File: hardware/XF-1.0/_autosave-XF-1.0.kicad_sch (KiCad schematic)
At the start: 9 parts

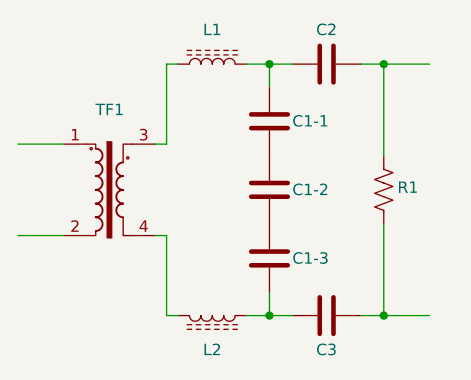
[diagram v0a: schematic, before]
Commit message: modified:   README.md 	new file:   hardware/XF-1.0/#auto_saved_files# 	new file:   hardware/XF-1.0/XF-1.0-backups/XF-1.0-2025-07-15_095716.zip 	modified:   hardware/XF-1.0/XF-1.0.kicad_sch 	new file:   hardware/XF-1.0/_autosave-XF-1.0.kicad_sch
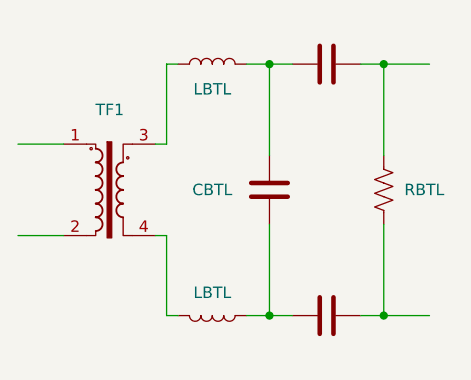
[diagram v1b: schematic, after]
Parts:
- removed C1-2, C1-3: 1nF, Capacitor_THT:C_Rect_L13.0mm_W8.0mm_P10.00mm_FKS3_FKP3_MKS4, symbol Device:C
- removed L1, L2: ~, Transformer_THT:Inductor-EE25, symbol Device:L_Ferrite
- added L1, L2: LBTL, symbol Device:L
- C3: renamed from C1-1; value 1nF -> CBTL
- R1: value R_US -> RBTL
- renumbered C2 to C1, C3 to C2
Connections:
- net at C2.1: now also C3.2, L2.2
- net at TF1.3: now also L1.1
- net at TF1.4: now also L2.1
- net at C1.1, C3.1: now also L1.2
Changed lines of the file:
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@@
 	(wire
 		(pts
-			(xy 149.86 59.69) (xy 149.86 62.23)
+			(xy 149.86 59.69) (xy 149.86 69.85)
 		)
 		(stroke
@@
 	(wire
 		(pts
+			(xy 149.86 77.47) (xy 149.86 87.63)
+		)
+		(stroke
+			(width 0)
+			(type default)
+		)
+	)
+	(wire
+		(pts
 			(xy 147.32 87.63) (xy 149.86 87.63)
 		)
@@
 		(pts
 			(xy 138.43 68.58) (xy 137.16 68.58)
-		)
-		(stroke
-			(width 0)
-			(type default)
-		)
-	)
-	(wire
-		(pts
-			(xy 149.86 85.09) (xy 149.86 87.63)
 		)
 		(stroke
@@
 		(on_board yes)
 		(dnp no)
-		(property "Reference" "C3"
+		(property "Reference" "C2"
 			(at 156.21 91.44 90)
 			(effects
@@
 					(size 1.27 1.27)
 				)
+				(hide yes)
 			)
 		)
@@
 			(project "XF-1.0"
 				(path "/12f985fe-55a3-431b-9b29-de85666dcd2b"
-					(reference "C3")
+					(reference "C2")
 					(unit 1)
 				)
@@
 	(symbol
 		(lib_id "Device:C")
-		(at 149.86 66.04 0)
-		(unit 1)
-		(exclude_from_sim no)
-		(in_bom yes)
-		(on_board yes)
-		(dnp no)
-		(property "Reference" "C1-1"
-			(at 152.4 66.04 0)
-			(effects
-				(font
-					(size 1.27 1.27)
-				)
-				(justify left)
-			)
-		)
-		(property "Value" "1nF"
-			(at 153.67 67.3099 0)
-			(effects
-				(font
-					(size 1.27 1.27)
-				)
-				(justify left)
-				(hide yes)
-			)
-		)
-		(property "Footprint" "Capacitor_THT:C_Rect_L13.0mm_W8.0mm_P10.00mm_FKS3_FKP3_MKS4"
-			(at 150.8252 69.85 0)
-			(effects
-				(font
-					(size 1.27 1.27)
-				)
-				(hide yes)
-			)
-		)
-		(property "Datasheet" "~"
-			(at 149.86 66.04 0)
-			(effects
-				(font
-					(size 1.27 1.27)
-				)
-				(hide yes)
-			)
-		)
-		(property "Description" "Unpolarized capacitor"
-			(at 149.86 66.04 0)
-			(effects
-				(font
-					(size 1.27 1.27)
-				)
-				(hide yes)
-			)
-		)
-		(pin "2"
-		)
-		(pin "1"
-		)
-		(instances
-			(project "XF-1.0"
-				(path "/12f985fe-55a3-431b-9b29-de85666dcd2b"
-					(reference "C1-1")
-					(unit 1)
-				)
-			)
-		)
-	)
-	(symbol
-		(lib_id "Device:C")
-		(at 149.86 81.28 0)
-		(unit 1)
-		(exclude_from_sim no)
-		(in_bom yes)
-		(on_board yes)
-		(dnp no)
-		(property "Reference" "C1-3"
-			(at 152.4 81.28 0)
-			(effects
-				(font
-					(size 1.27 1.27)
-				)
-				(justify left)
-			)
-		)
-		(property "Value" "1nF"
-			(at 153.67 82.5499 0)
-			(effects
-				(font
-					(size 1.27 1.27)
-				)
-				(justify left)
-				(hide yes)
-			)
-		)
-		(property "Footprint" "Capacitor_THT:C_Rect_L13.0mm_W8.0mm_P10.00mm_FKS3_FKP3_MKS4"
-			(at 150.8252 85.09 0)
-			(effects
-				(font
-					(size 1.27 1.27)
-				)
-				(hide yes)
-			)
-		)
-		(property "Datasheet" "~"
-			(at 149.86 81.28 0)
-			(effects
-				(font
-					(size 1.27 1.27)
-				)
-				(hide yes)
-			)
-		)
-		(property "Description" "Unpolarized capacitor"
-			(at 149.86 81.28 0)
-			(effects
-				(font
-					(size 1.27 1.27)
-				)
-				(hide yes)
-			)
-		)
-		(pin "2"
-		)
-		(pin "1"
-		)
-		(instances
-			(project "XF-1.0"
-				(path "/12f985fe-55a3-431b-9b29-de85666dcd2b"
-					(reference "C1-3")
-					(unit 1)
-				)
-			)
-		)
-	)
-	(symbol
-		(lib_id "Device:C")
 		(at 149.86 73.66 0)
 		(unit 1)
@@
 		(on_board yes)
 		(dnp no)
-		(property "Reference" "C1-2"
+		(property "Reference" "C3"
 			(at 152.4 73.66 0)
 			(effects
@@
 				)
 				(justify left)
-			)
-		)
-		(property "Value" "1nF"
-			(at 153.67 74.9299 0)
-			(effects
-				(font
-					(size 1.27 1.27)
-				)
-				(justify left)
-				(hide yes)
+				(hide yes)
+			)
+		)
+		(property "Value" "CBTL"
+			(at 143.51 73.66 0)
+			(effects
+				(font
+					(size 1.27 1.27)
+				)
 			)
 		)
@@
 		(property "Description" "Unpolarized capacitor"
 			(at 149.86 73.66 0)
+			(effects
+				(font
+					(size 1.27 1.27)
+				)
+				(hide yes)
+			)
+		)
+		(pin "2"
+		)
+		(pin "1"
+		)
+		(instances
+			(project "XF-1.0"
+				(path "/12f985fe-55a3-431b-9b29-de85666dcd2b"
+					(reference "C3")
+					(unit 1)
+				)
+			)
+		)
+	)
+	(symbol
+		(lib_id "Device:L")
+		(at 143.51 59.69 90)
+		(unit 1)
+		(exclude_from_sim no)
+		(in_bom yes)
+		(on_board yes)
+		(dnp no)
+		(property "Reference" "L1"
+			(at 143.51 55.88 90)
+			(effects
+				(font
+					(size 1.27 1.27)
+				)
+				(hide yes)
+			)
+		)
+		(property "Value" "LBTL"
+			(at 143.51 62.484 90)
+			(effects
+				(font
+					(size 1.27 1.27)
+				)
+			)
+		)
+		(property "Footprint" ""
+			(at 143.51 59.69 0)
+			(effects
+				(font
+					(size 1.27 1.27)
+				)
+				(hide yes)
+			)
+		)
+		(property "Datasheet" "~"
+			(at 143.51 59.69 0)
+			(effects
+				(font
+					(size 1.27 1.27)
+				)
+				(hide yes)
+			)
+		)
+		(property "Description" "Inductor"
+			(at 143.51 59.69 0)
 			(effects
 				(font
@@
 			(project ""
 				(path "/12f985fe-55a3-431b-9b29-de85666dcd2b"
-					(reference "C1-2")
+					(reference "L1")
 					(unit 1)
 				)
@@
 	)
 	(symbol
-		(lib_id "Device:L_Ferrite")
+		(lib_id "Device:L")
 		(at 143.51 87.63 90)
 		(mirror x)
@@
 					(size 1.27 1.27)
 				)
-			)
-		)
-		(property "Value" "~"
-			(at 143.51 91.44 90)
-			(effects
-				(font
-					(size 1.27 1.27)
-				)
-				(hide yes)
-			)
-		)
-		(property "Footprint" "Transformer_THT:Inductor-EE25"
+				(hide yes)
+			)
+		)
+		(property "Value" "LBTL"
+			(at 143.51 85.09 90)
+			(effects
+				(font
+					(size 1.27 1.27)
+				)
+			)
+		)
+		(property "Footprint" ""
 			(at 143.51 87.63 0)
 			(effects
@@
 			)
 		)
-		(property "Description" "Inductor with ferrite core"
+		(property "Description" "Inductor"
 			(at 143.51 87.63 0)
 			(effects
@@
 		(on_board yes)
 		(dnp no)
-		(property "Reference" "C2"
+		(property "Reference" "C1"
 			(at 156.21 55.88 90)
 			(effects
@@
 					(size 1.27 1.27)
 				)
+				(hide yes)
 			)
 		)
@@
 			(project "XF-1.0"
 				(path "/12f985fe-55a3-431b-9b29-de85666dcd2b"
-					(reference "C2")
-					(unit 1)
-				)
-			)
-		)
-	)
-	(symbol
-		(lib_id "Device:L_Ferrite")
-		(at 143.51 59.69 90)
-		(unit 1)
-		(exclude_from_sim no)
-		(in_bom yes)
-		(on_board yes)
-		(dnp no)
-		(property "Reference" "L1"
-			(at 143.51 55.88 90)
-			(effects
-				(font
-					(size 1.27 1.27)
-				)
-			)
-		)
-		(property "Value" "~"
-			(at 143.51 55.88 90)
-			(effects
-				(font
-					(size 1.27 1.27)
-				)
-				(hide yes)
-			)
-		)
-		(property "Footprint" "Transformer_THT:Inductor-EE25"
-			(at 143.51 59.69 0)
-			(effects
-				(font
-					(size 1.27 1.27)
-				)
-				(hide yes)
-			)
-		)
-		(property "Datasheet" "~"
-			(at 143.51 59.69 0)
-			(effects
-				(font
-					(size 1.27 1.27)
-				)
-				(hide yes)
-			)
-		)
-		(property "Description" "Inductor with ferrite core"
-			(at 143.51 59.69 0)
-			(effects
-				(font
-					(size 1.27 1.27)
-				)
-				(hide yes)
-			)
-		)
-		(pin "2"
-		)
-		(pin "1"
-		)
-		(instances
-			(project ""
-				(path "/12f985fe-55a3-431b-9b29-de85666dcd2b"
-					(reference "L1")
+					(reference "C1")
 					(unit 1)
 				)
@@
 				)
 				(justify left)
-			)
-		)
-		(property "Value" "R_US"
-			(at 165.1 74.9299 0)
+				(hide yes)
+			)
+		)
+		(property "Value" "RBTL"
+			(at 164.846 73.66 0)
 			(effects
 				(font
@@
 				)
 				(justify left)
-				(hide yes)
-			)
-		)
+			)
+		)

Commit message: modified:   .DS_Store 	modified:   README.md 	modified:   hardware/XF-1.0/_autosave-XF-1.0.kicad_sch 	new file:   pic/Type-1 Butterworth Filter.png
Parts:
- removed TF1: ~, Transformer_THT:EE35-1P-1S-Vertical-2143, symbol Transformer:ER35-1P-1S
- added C4: CL = 2 • CBTL, Capacitor_THT:C_Rect_L13.0mm_W8.0mm_P10.00mm_FKS3_FKP3_MKS4, symbol Device:C
- added C5: 4.7nF, Capacitor_THT:C_Rect_L13.0mm_W8.0mm_P10.00mm_FKS3_FKP3_MKS4, symbol Device:C
- added L3: LBTL, symbol Device:L
- added R2: RBTL, symbol Device:R_US
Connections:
- new net: C4.1, C5.1, L3.2
- new net: C5.2, R2.1
- new net GNDREF: C4.2, R2.2
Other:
- note added: "Single-Ended Equivalent"
- note added: "Type-1 Butterworth Filter"

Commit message: modified:   Ferrite Transformer Calculation.xlsx 	modified:   README.md 	deleted:    hardware/XF-1.0/XF-1.0-backups/XF-1.0-2025-07-15_095716.zip 	new file:   hardware/XF-1.0/XF-1.0-backups/XF-1.0-2025-07-15_145509.zip 	new file:   hardware/XF-1.0/XF-1.0-backups/XF-1.0-2025-07-15_150114.zip 	new file:   hardware/XF-1.0/XF-1.0-backups/XF-1.0-2025-07-15_150614.zip 	new file:   hardware/XF-1.0/XF-1.0-backups/XF-1.0-2025-07-15_151503.zip 	new file:   hardware/XF-1.0/XF-1.0-backups/XF-1.0-2025-07-15_152320.zip 	new file:   hardware/XF-1.0/XF-1.0-backups/XF-1.0-2025-07-15_154638.zip 	modified:   hardware/XF-1.0/XF-1.0.kicad_pcb 	modified:   hardware/XF-1.0/XF-1.0.kicad_prl 	modified:   hardware/XF-1.0/XF-1.0.kicad_pro 	modified:   hardware/XF-1.0/XF-1.0.kicad_sch 	modified:   hardware/XF-1.0/_autosave-XF-1.0.kicad_sch 	modified:   hardware/XF-1.0/fp-info-cache
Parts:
- removed C4: CL = 2 • CBTL, Capacitor_THT:C_Rect_L13.0mm_W8.0mm_P10.00mm_FKS3_FKP3_MKS4, symbol Device:C
- removed C5: 4.7nF, Capacitor_THT:C_Rect_L13.0mm_W8.0mm_P10.00mm_FKS3_FKP3_MKS4, symbol Device:C
- removed L3: LBTL, symbol Device:L
- removed R2: RBTL, symbol Device:R_US
- added CN1, CN2: Conn_01x02, Connector_Molex:Molex_KK-396_5273-03A_1x03_P3.96mm_Vertical_2, symbol Connector_Generic:Conn_01x02
- added H1, H2, H3, H4: ~, MountingHole:MountingHole_3mm_Pad, symbol Mechanical:MountingHole_Pad
- added XF1: ~, Transformer_THT:Transformer_Toroid_Horizontal_OD40_ID23_H15, symbol Transformer:TRANSF1
- C1: renamed from C3; value CBTL -> 2.7nF
- L1, L2: value LBTL -> 29µH; footprint (none) -> Inductor_THT:L_Radial_Multilayer_D8.0mm_P12.70mm
- renumbered C1 to C2, C2 to C3
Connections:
- net at C3.2, R1.2: now also CN2.2 (Pin_2)
- net at L1.1: now also XF1.4
- net at L2.1: now also XF1.3
- net at C2.2, R1.1: now also CN2.1 (Pin_1)
- new net: CN1.1 (Pin_1), XF1.1
- new net: CN1.2 (Pin_2), XF1.2
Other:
- note removed: "Single-Ended Equivalent"
- note removed: "Type-1 Butterworth Filter"
